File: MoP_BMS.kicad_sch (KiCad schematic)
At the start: 53 parts, among them J10 TH_CONN, J11 PACK+EN, J12 PACK-EN, J13 PMON, J14 CTRL, J8 Balance, J9 BAT, Q2 SSM3K341TU_LF, Q3 SSM3K341TU_LF, SW1 BMS_BOOT, U12 BQ76920PW, U13 BQ76200PW

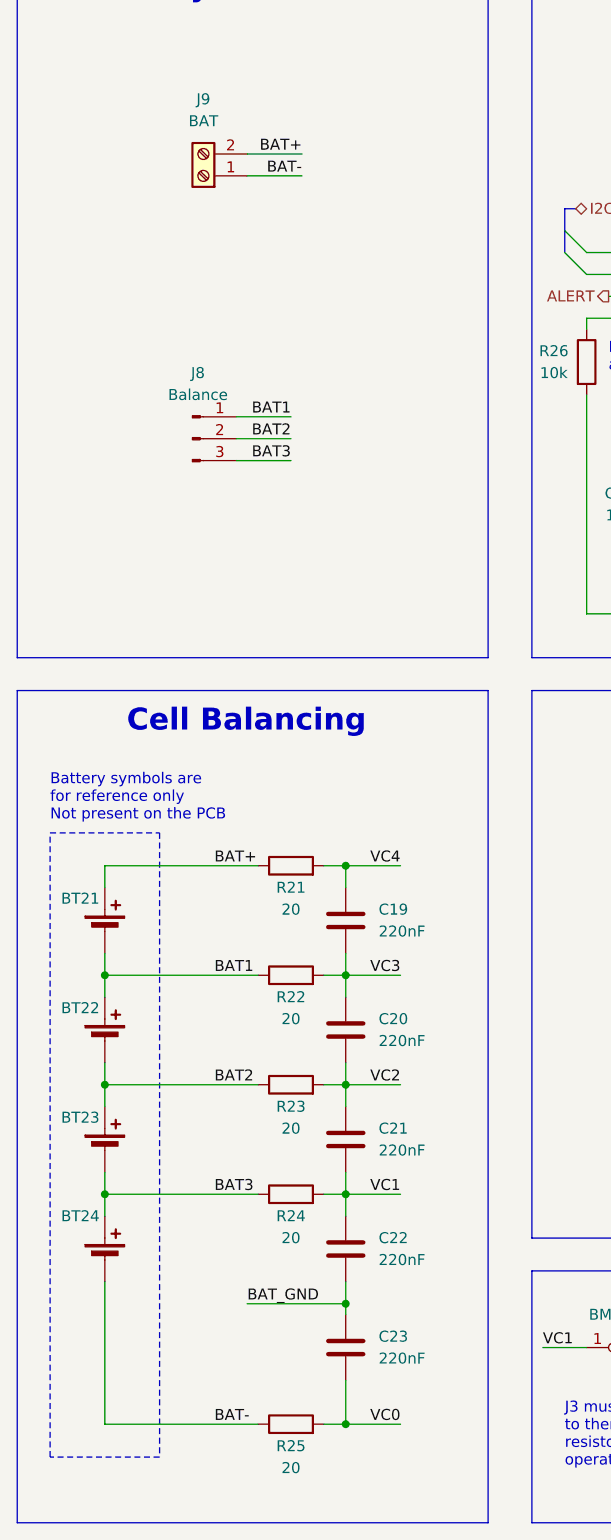
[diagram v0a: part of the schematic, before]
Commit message: changed ref designators to be consistent accross sheets
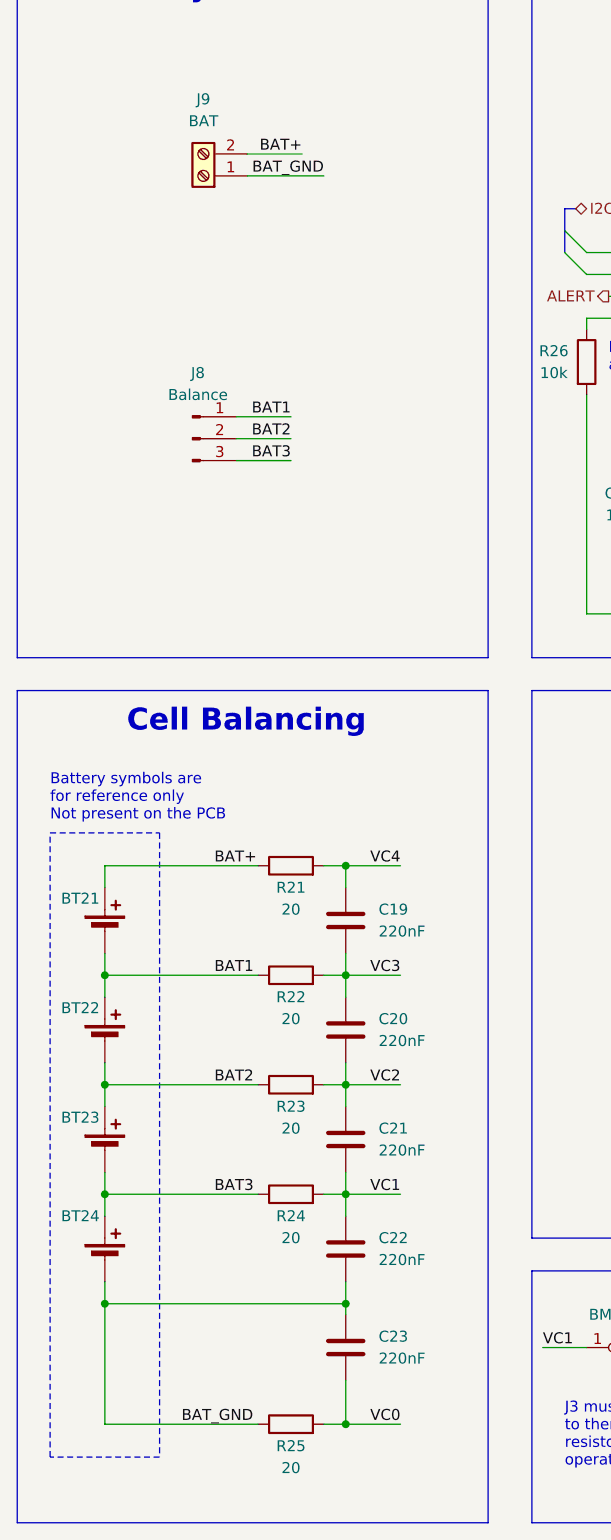
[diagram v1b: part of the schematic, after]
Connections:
- net BAT- is gone; now on net BAT_GND: BT24.2 (-), J9.1 (Pin_1), R25.1
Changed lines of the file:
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@@
+	)
+	(junction
+		(at 25.4 170.18)
+		(diameter 0)
+		(color 0 0 0 0)
 	)
 	(junction
@@
 	(wire
 		(pts
-			(xy 41.91 39.37) (xy 48.26 39.37)
+			(xy 41.91 39.37) (xy 50.8 39.37)
 		)
 		(stroke
@@
 	(wire
 		(pts
+			(xy 25.4 170.18) (xy 53.34 170.18)
+		)
+		(stroke
+			(width 0)
+			(type default)
+		)
+	)
+	(wire
+		(pts
 			(xy 88.9 53.34) (xy 88.9 55.88)
 		)
@@
 	(wire
 		(pts
+			(xy 25.4 170.18) (xy 25.4 184.15)
+		)
+		(stroke
+			(width 0)
+			(type default)
+		)
+	)
+	(wire
+		(pts
 			(xy 115.57 90.17) (xy 115.57 83.82)
 		)
@@
 	(wire
 		(pts
-			(xy 41.91 170.18) (xy 53.34 170.18)
-		)
-		(stroke
-			(width 0)
-			(type default)
-		)
-	)
-	(wire
-		(pts
 			(xy 195.58 148.59) (xy 204.47 148.59)
 		)
@@
 	(wire
 		(pts
-			(xy 25.4 167.64) (xy 25.4 184.15)
+			(xy 25.4 167.64) (xy 25.4 170.18)
 		)
 		(stroke
@@
 		)
 	)
-	(label "BAT_GND"
-		(at 41.91 170.18 0)
-		(fields_autoplaced yes)
-		(effects
-			(font
-				(size 1.27 1.27)
-			)
-			(justify left bottom)
-		)
-	)
 	(label "CP_EN"
 		(at 276.86 53.34 180)
@@
 		)
 	)
-	(label "BAT-"
-		(at 48.26 39.37 180)
+	(label "BAT_GND"
+		(at 50.8 39.37 180)
 		(fields_autoplaced yes)
 		(effects
@@
 		)
 	)
-	(label "BAT-"
-		(at 38.1 184.15 0)
-		(fields_autoplaced yes)
-		(effects
+	(label "BAT_GND"
+		(at 34.29 184.15 0)
+		(fields_autoplaced yes)
+		(effects
